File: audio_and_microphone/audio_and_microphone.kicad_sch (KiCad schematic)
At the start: 33 parts, among them J1 Conn_01x02, J10 Conn_01x03_Socket, J11 Conn_01x02, J2 Conn_01x02, J3 Conn_01x02, J4 Conn_01x02, J5 Conn_01x10_MountingPin, J6 Conn_01x08_MountingPin, J7 Conn_01x08_MountingPin, J8 Conn_01x06_MountingPin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

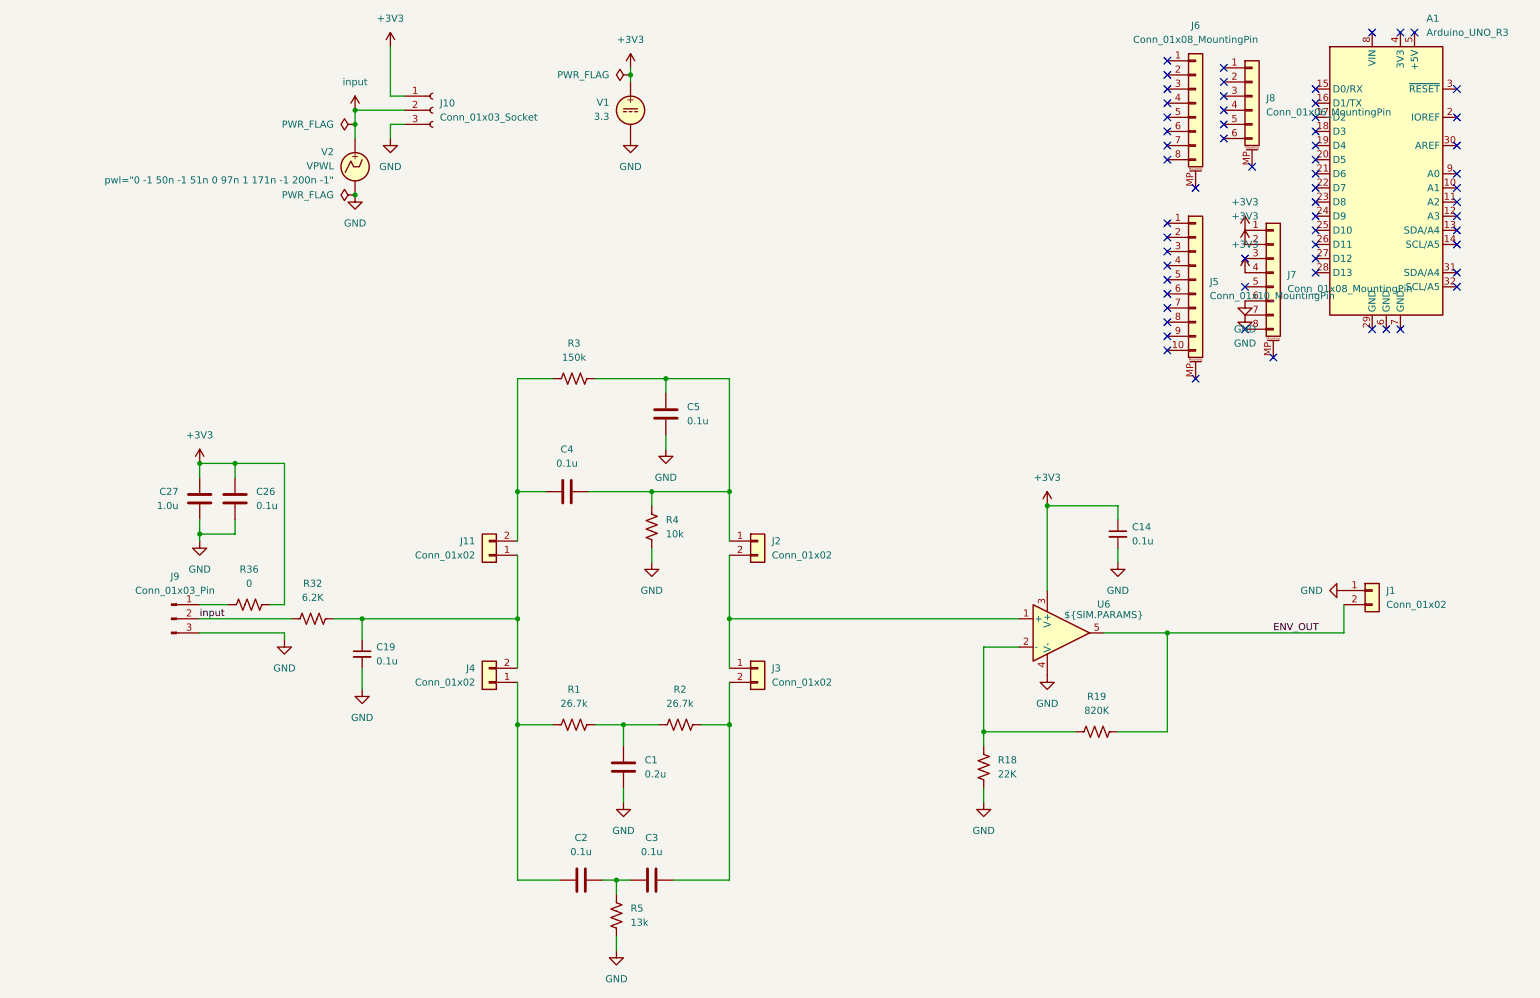
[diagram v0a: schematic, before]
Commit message: labeled schematic and fixed track widths in pcb. passed drc
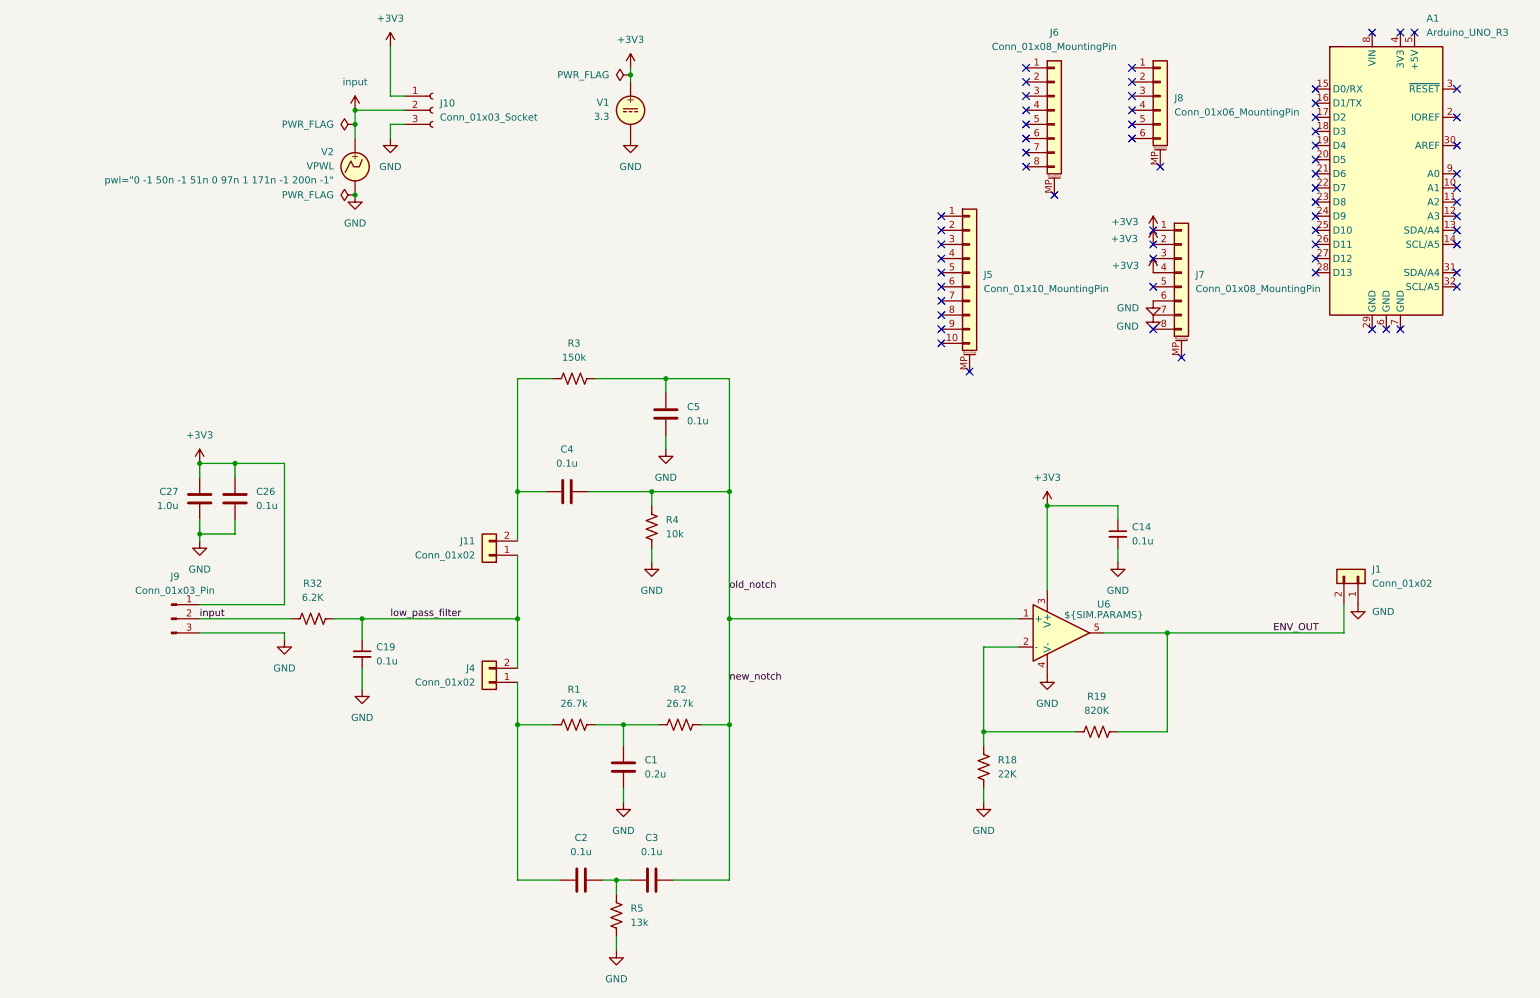
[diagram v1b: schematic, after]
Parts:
- removed J2, J3: Conn_01x02, Connector_PinHeader_2.54mm:PinHeader_1x02_P2.54mm_Vertical, symbol Connector_Generic:Conn_01x02
- removed R36: 0, RC0603FR_072KL:R0603, symbol Device:R_US
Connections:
- net +3V3: now also J9.1 (Pin_1)
- net new_notch: now reaches C4.2, C5.1, R3.2, R4.1
- net new_notch: now also C3.2, R2.2, U6.1 (+)
- net low_pass_filter: now reaches C19.1, J11.1 (Pin_1), J4.2 (Pin_2), R32.1
- no-connect marks 62 -> 64
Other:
- moved on the sheet: J1, J5, J6, J7, J8

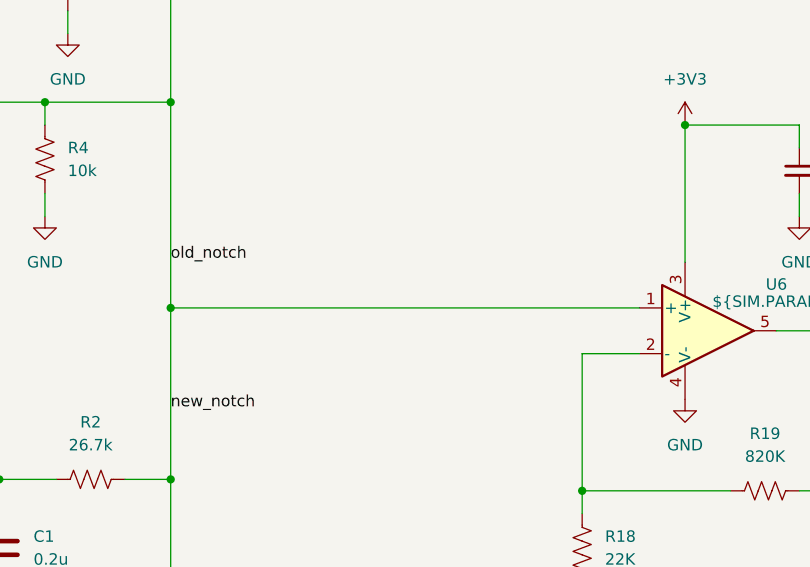
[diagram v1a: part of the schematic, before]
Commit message: added additional test point and fixed pcb words to be silkscreen
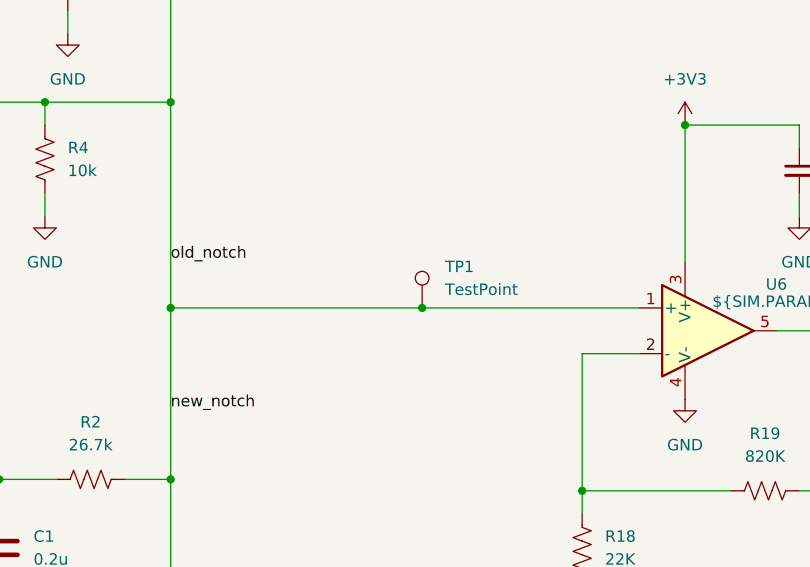
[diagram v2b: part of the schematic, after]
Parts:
- added TP1: TestPoint, TestPoint:TestPoint_Keystone_5000-5004_Miniature, symbol Connector:TestPoint
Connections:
- net new_notch: now also TP1.1
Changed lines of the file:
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@@
 	)
 	(junction
+		(at 170.18 123.19)
+		(diameter 0)
+		(color 0 0 0 0)
+	)
+	(junction
 		(at 142.24 100.33)
 		(diameter 0)
@@
 	(wire
 		(pts
+			(xy 170.18 123.19) (xy 194.31 123.19)
+		)
+		(stroke
+			(width 0)
+			(type default)
+		)
+	)
+	(wire
+		(pts
 			(xy 74.93 34.29) (xy 74.93 36.83)
 		)
@@
 	(wire
 		(pts
-			(xy 142.24 123.19) (xy 194.31 123.19)
+			(xy 142.24 123.19) (xy 170.18 123.19)
 		)
 		(stroke
@@
 					(unit 1)
 				)
+			)
+		)
+	)
+	(symbol
+		(lib_id "Connector:TestPoint")
+		(at 170.18 123.19 0)
+		(unit 1)
+		(exclude_from_sim no)
+		(in_bom yes)
+		(on_board yes)
+		(dnp no)
+		(fields_autoplaced yes)
+		(property "Reference" "TP1"
+			(at 172.72 118.6179 0)
+			(effects
+				(font
+					(size 1.27 1.27)
+				)
+				(justify left)
+			)
+		)
+		(property "Value" "TestPoint"
+			(at 172.72 121.1579 0)
+			(effects
+				(font
+					(size 1.27 1.27)
+				)
+				(justify left)
+			)
+		)
+		(property "Footprint" "TestPoint:TestPoint_Keystone_5000-5004_Miniature"
+			(at 175.26 123.19 0)
+			(effects
+				(font
+					(size 1.27 1.27)
+				)
+				(hide yes)
+			)
+		)
+		(property "Datasheet" "~"
+			(at 175.26 123.19 0)
+			(effects
+				(font
+					(size 1.27 1.27)
+				)
+				(hide yes)
+			)
+		)
+		(property "Description" "test point"
+			(at 170.18 123.19 0)
+			(effects
+				(font
+					(size 1.27 1.27)
+				)
+				(hide yes)
+			)
+		)
+		(pin "1"
+		)
+		(instances
+			(project ""
+				(path "/6041ce46-c287-4741-ac80-b7b1d4df1348"
+					(reference "TP1")
+					(unit 1)
+				)
